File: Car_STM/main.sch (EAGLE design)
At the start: 66 parts, among them IC1 BLUEPILL550, IC2 7805TV, K1 G2R, K2 G2R, K3 TF2-L2-9V, Q1 BC557, Q2 BC557, T1 BC547, T2 BC547, T3 BC547, T4 BC547, X1 1751251, X10 1751251, X11 1751251, X2 1751248, X3 1751264, X4 1751251, X5 1751303, X6 1751248, X7 1751248, X8 1751248, X9 1751264

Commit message: V1.1 Schematic ended
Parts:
- removed C2: 100n, resistor:C-EUC2012
- removed IC2: 7805TV, linear:7805TV
- removed K2: G2R, relay:G2R
- removed T1, T2, T3, T4: BC547, transistor:BC547
- removed T5, T6, T7, T8: (no value), transistor:-NPN-TO92-ECB
- removed X11: 1751251, con-phoenix-350:1751251
- removed X8: 1751248, con-phoenix-350:1751248
- added 12V_IN: (no value), con-ptr500:AK500/3
- added D5: (no value), diode:DIODE-DO-214AC
- added D6: LL4148, _hhn_diodes_smd:LL4148
- added FUSE1: F0.315, resistor:R-EU_R2512
- added FUSE2: F1.0, resistor:R-EU_R2512
- added K4: S22, Stworzone:S22
- added Q10, Q11, Q12, Q13, Q14, Q15, Q16, Q5, Q6, Q7: BC817-40LT1SMD, transistor-npn:BC817-40LT1SMD
- added Q18, Q3, Q4, Q8: BSS123, transistor-small-signal:BSS123
- added Q9: IRFR5305, transistor-power:IRFR5305
- added R25, R29: 2k2, resistor:R-EU_R0805
- added R26, R27: 240, resistor:R-EU_R0805
- added R30: 100k, resistor:R-EU_R0805
- C1: value 100n -> 100u; device resistor:C-EUC2012 -> resistor:CPOL-EUE2,5-6E
- C3: value 100u -> (none); device resistor:CPOL-EUE2,5-6E -> Cap-Gold:CAP-13,5
- D3: value BAS15 -> (none); device diode:BAS15 -> diode:DIODE-DO-214AC
- D4: value BAS15 -> LL4148; device diode:BAS15 -> _hhn_diodes_smd:LL4148
- K1: value G2R -> G2RE; device relay:G2R -> relay:G2RE
- Q1, Q2: value BC557 -> BC807-40LT1SMD; device transistor-pnp:BC557 -> transistor-pnp:BC807-40LT1SMD
- R1, R2: value 2k2 -> 100k; device resistor:R-EU_0204/7 -> resistor:R-EU_R0805
- R10, R6: value 1k8 -> 6k8; device rcl:R-EU_0204/5 -> resistor:R-EU_R0805
- R12: value 2k2 -> 100; device resistor:R-EU_0204/7 -> resistor:R-EU_R0805
- R13, R14, R24: device resistor:R-EU_0204/7 -> resistor:R-EU_R0805
- R15: value 200 -> 240; device pot:TRIM_EU-B25P -> resistor:R-EU_R0805
- R16: value 70 -> 100; device resistor:R-EU_0204/7 -> resistor:R-EU_R0805
- R17, R3, R4: value 2k2 -> 1k8; device resistor:R-EU_0204/7 -> resistor:R-EU_R0805
- R18: value 2k2 -> 6k8; device resistor:R-EU_0204/7 -> resistor:R-EU_R0805
- R19: value 6k8 -> 1k8; device rcl:R-EU_0204/5 -> resistor:R-EU_R0805
- R20: value 1k8 -> 2k2; device rcl:R-EU_0204/5 -> resistor:R-EU_R0805
- R21, R22: value 100k -> 100; device resistor:R-EU_0204/7 -> resistor:R-EU_R0805
- R23: value 0 -> 2k2; device resistor:R-EU_0204/7 -> resistor:R-EU_R0805
- R5: device rcl:R-EU_0204/5 -> resistor:R-EU_R0805
- R9: value 6k8 -> 2k2; device rcl:R-EU_0204/5 -> resistor:R-EU_R0805
- X1: value 1751251 -> (none); device con-phoenix-350:1751251 -> con-ptr500:AK500/3
- X10: value 1751251 -> 1751264; device con-phoenix-350:1751251 -> con-phoenix-350:1751264
- X4: value 1751251 -> (none); device con-phoenix-350:1751251 -> con-ptr500:AK500/2
- X6: value 1751248 -> 1751264; device con-phoenix-350:1751248 -> con-phoenix-350:1751264
- X9: value 1751264 -> 1751277; device con-phoenix-350:1751264 -> con-phoenix-350:1751277
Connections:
- removed net +5V: C1.1, C3.+, IC2.VO, X3-3.K
- removed net BOOT_OPEN: IC1.PB7, R17.2
- removed net LOCK: IC1.PB8, R18.2
- removed net OBD_RX: IC1.PA9, X3-2.K
- removed net OBD_TX: IC1.PA10, X3-1.K
- removed net POWER_ON: R12.2
- removed net RFID_RS: IC1.PA15, X5-7.K
- new net 12_VOL: IC1.PA1, R18.1, R19.2
- new net AUDIO1: IC1.PA6, R25.1
- new net AUDIO2: IC1.PA7, R24.2
- new net BT_MODE: IC1.PB1, R29.1
- new net BT_POW: IC1.PB0, R22.1
- new net CAN_POW: IC1.PB7, R12.1
- new net CAN_RX: IC1.PB8, X3-1.K
- new net CAN_TX: IC1.PB9, X3-2.K
- new net MAIN_POW: D6.A, IC1.PC13
- new net MIR_POW: IC1.PC15, R9.1
- new net N$30: K31.O, X10-2.K
- new net N$31: K31.P, K32.S
- new net N$32: K32.O, X10-1.K
- new net N$33: K32.P, X10-4.K
- new net N$34: K3S.+, R27.1
- new net N$35: K3R.+, R26.1
- new net N$36: K3S.-, Q6.C
- new net N$37: K3R.-, Q7.C
- new net N$38: Q6.B, R25.2
- new net N$39: Q8.D, X9-4.K
- new net N$40: FUSE1.1, FUSE2.1, Q9.D
- new net N$41: Q7.B, R24.1
- new net N$42: R29.2, X9-5.K
- new net N$43: Q10.B, R20.1, R23.1
- new net N$44: Q10.C, Q9.G, R30.1
- new net N$45: D6.C, R23.2
- new net N$46: C7.1, FUSE1.2, LM1084.VI
- new net N$47: Q18.D, U$1.GND
- new net N$48: K4G$1.P, X1-3.KL
- new net N$49: C4.1, FUSE2.2, LM317.VI
- new net N$51: Q18.G, R21.2
- new net SIM_POW: IC1.PB6, R21.1
- net +12V: now also D5.C, K4G$1.S, K4G$2.1, Q9.S, R26.2, R27.2, R30.2; no longer C7.1, D4.C, K12.S, K21.1, LM1084.VI, R21.1, R22.1, X1-1.K
- net +3V3: now also C3.+, IC1.3VB, R15.2, X3-3.K, X5-7.K, X6-1.K; no longer R15.A, X10-1.K, X11-1.K
- net 12_IN: now also D4.A, IC1.PA0, R10.2, R17.1; no longer IC1.PB0, R19.1, R20.2
- net BUZZER: now also IC1.PA11
- net FUEL_POMP: now also IC1.PC14, R13.1; no longer IC1.PA8, R13.2
- net GND: now also 12V_IN-3.KL, C1.-, Q10.E, Q11.E, Q12.E, Q15.E, Q16.E, Q18.S, Q3.S, Q4.S, Q5.E, Q6.E, Q7.E, Q8.S, R17.2, R19.1, R3.2, R4.2, X6-4.K; no longer C1.2, C2.2, IC2.GND, R10.1, R20.1, R23.2, R6.1, T1.E, T2.E, T3.E, T4.E, T5.E, T6.E, T8.E, U$1.GND, X10-2.K, X11-2.K, X3-4.K, X4-3.K, X9-4.K
- net L1: now also IC1.PA2; no longer IC1.PA12, R3.2
- net L2: now also IC1.PA3, R2.1; no longer IC1.PA11, R2.2, R4.2
- net LOCK_CLOSE: now also R4.1; no longer R5.1
- net LOCK_OPEN: now also IC1.PB5, R3.1, R5.2; no longer IC1.PB3, R10.2, R9.1
- net M1: now also X6-2.K; no longer X10-3.K
- net M2: now also X6-3.K; no longer X11-3.K
- net N$1: now also 12V_IN-1.KL, R18.2; no longer X4-1.K
- net N$10: now also D4.C, R20.2; no longer R3.1, T2.B
- net N$12: now also Q3.G, R12.2; no longer C2.1, C4.1, IC2.VI, K12.P, LM317.VI
- net N$13: now also Q8.G, R22.2; no longer D4.A, K11.2, T3.C
- net N$15: now also Q3.D, X3-4.K; no longer R12.1, T3.B
- net N$16: now also K11.2, Q16.C; no longer K21.2, T4.C
- net N$17: now also Q16.B, R13.2; no longer R13.1, T4.B
- net N$18: now also K12.S, K12.S@1, X4-1.KL; no longer K22.S, X6-1.K
- net N$19: now also K12.P, K12.P@1, X4-2.KL; no longer K22.P, X6-2.K
- net N$2: now also 12V_IN-2.KL, R10.1; no longer R19.2, X4-2.K
- net N$21: now also Q4.D; no longer T8.C
- net N$22: now also K31.S, X10-3.K; no longer R15.S, R16.2
- net N$23: now also Q14.B, R1.1; no longer R17.1, T6.B
- net N$24: now also Q5.B; no longer T5.B
- net N$25: now also Q13.B, R2.2; no longer R21.2, T6.C, X8-1.K
- net N$26: now also Q11.B, Q14.E; no longer R18.1, T7.B
- net N$27: now also Q4.G, R16.2; no longer R24.1, T8.B
- net N$28: now also Q15.B, R9.2; no longer R22.2, T7.C, X8-2.K
- net N$29: now also D5.A, K4G$2.2, Q15.C; no longer R23.1, T7.E
- net N$3: now also R6.1; no longer R5.2
- net N$4: now also Q11.C, X1-2.KL; no longer T1.C, X1-2.K
- net N$5: now also Q12.C, X1-1.KL; no longer T2.C, X1-3.K
- net N$6: now also R5.1; no longer R9.2
- net N$7: now also Q14.C, Q2.B; no longer Q1.B, R1.1
- net N$8: now also Q1.B, Q13.C; no longer Q2.B, R4.1
- net N$9: now also Q12.B, Q13.E; no longer R2.1, T1.B
- net RFID_INT: now also IC1.PA12; no longer IC1.PB5
- net RFID_POW: now also IC1.PA15, R16.1; no longer R24.2
- net SIM_RS: now also IC1.PA8; no longer IC1.PA1
- net SIM_RX: now also IC1.PA9; no longer IC1.PA2
- net SIM_TX: now also IC1.PA10; no longer IC1.PA3
- net VCC: now also C1.+
- net WATER: now also IC1.PB3, Q5.C, R15.1; no longer IC1.PB6, R16.1, T5.C
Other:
- moved on the sheet: C4, C5, C6, C7, C8, D1, D2, K1, K3, LM1084, LM317, Q1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

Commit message: V1.2 Two boards from one.
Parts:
- removed IC1: BLUEPILL550, STM32BluePill:BLUEPILL550
- removed LM1084: 3V3, linear:317T
- added C10, C11, C12, C13, C2, C33, C9: 100nF, eagle-ltspice:CC2012
- added C14, C15: 100u, resistor:CPOL-EUE2,5-6E
- added C29, C30: 10pF, eagle-ltspice:CC2012
- added C31, C32: 6,8pF, eagle-ltspice:CC2012
- added D10, D11, D12, D13, D14, D15, D16, D17, D7, D8, D9: (no value), diode:DIODE-DO-214AC
- added JP1: (no value), pinhead:PINHD-1X4
- added K10, K11, K2: HY1-12V, relay:HY1-12V
- added K12, K13: G2RE, relay:G2RE
- added K14: TF2-L2-9V, relay:TF2-L2-9V
- added K5, K6, K7, K8, K9: S22, Stworzone:S22
- added LM1086: 3V3, v-reg:LM317BD2T
- added Q17: 8MHz, crystal:CRYSTALHC49UP
- added Q19: MC-306 - 32,768kHz, crystal:MC-306
- added Q20, Q21, Q22, Q23, Q24, Q25, Q26, Q27, Q28, Q29, Q30, Q31: BC817-40LT1SMD, transistor-npn:BC817-40LT1SMD
- added R28, R31, R32, R33, R34, R35, R36, R37, R38, R39, R40, R41: 2k2, resistor:R-EU_R0805
- added R42, R43: 120, resistor:R-EU_R0805
- added S1: SWITCH-MOMENTARY-2SMD-4, SparkFun-Electromechanical:SWITCH-MOMENTARY-2SMD-4
- added SJ1, SJ2, SJ3, SJ4: (no value), jumper:SJ
- added U$2, U$3, U$4, U$5: JACK_3.5, Stworzone:JACK_3.5
- added U$6, U$7: D2_HEAT, Stworzone:D2_HEAT
- added U1: STM32F10XRXT6, stm32:STM32F10XRXT6
- added X11, X13: 1751248, con-phoenix-350:1751248
- added X12, X17, X18: 1751251, con-phoenix-350:1751251
- added X14, X15, X16, X21: (no value), con-ptr500:AK500/2
- added X19, X20, X8: (no value), con-ptr500:AK500/3
- D1, D2: value 1N4004 -> (none); device diode:1N4004 -> diode:DIODE-P6-15
- LM317: value 4v2 -> 4V2; device linear:317T -> v-reg:LM317BD2T
- R26, R27: value 240 -> 120
- X1: value (none) -> 1751248; device con-ptr500:AK500/3 -> con-phoenix-350:1751248
- X10: value 1751264 -> (none); device con-phoenix-350:1751264 -> con-ptr500:AK500/2
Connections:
- removed net N$1: 12V_IN-1.KL, D1.A, R18.2
- new net AD_REL1: R33.1, U1PORTC_L.PC5
- new net AD_REL2: R34.1, U1PORTC_L.PC6
- new net AD_REL3: R35.1, U1PORTC_L.PC7
- new net AD_REL4: R36.1, U1PORTC_H.PC8
- new net AD_REL5: R37.1, U1PORTC_H.PC9
- new net AD_REL6: R38.1, U1PORTC_H.PC10
- new net AD_REL7: R39.1, U1PORTC_H.PC11
- new net BOOT0: SJ2.1, SJ3.1, U1RESET.BOOT0
- new net BOOT1: SJ1.1, SJ4.1, U1PORTB_L.PB2
- new net BT_STER: R28.1, U1PORTC_H.PC13
- new net CHAR_POW: R31.1, U1PORTC_L.PC4
- new net C_OSC1: C31.2, Q19.1, U1PORTC_H.PC14
- new net C_OSC2: C32.2, Q19.2, U1PORTC_H.PC15
- new net DAY_LIGHT: R32.1, U1PORTC_H.PC12
- new net LIGHT: U1PORTC_L.PC0, X12-2.K
- new net N$100: K141.P, U$5.2
- new net N$101: K142.P, U$5.5
- new net N$50: Q31.B, R41.1
- new net N$52: D7.A, K21.2, Q20.C
- new net N$53: Q20.B, R28.2
- new net N$54: D11.C, K6G$1.P, X13-1.K
- new net N$55: Q26.B, R36.2
- new net N$56: D8.A, K5G$2.2, Q21.C
- new net N$57: K22.S, X11-2.K
- new net N$58: K22.P, K22.P@1, X11-1.K
- new net N$59: Q21.B, R31.2
- new net N$60: D9.A, K6G$2.2, Q22.C
- new net N$61: Q22.B, R32.2
- new net N$62: D10.A, K7G$2.2, Q23.C
- new net N$63: Q23.B, R33.2
- new net N$64: K5G$1.P, X8-2.KL
- new net N$65: K7G$1.P, X14-1.KL
- new net N$66: D14.A, K101.2, Q26.C
- new net N$67: D12.A, K8G$2.2, Q24.C
- new net N$68: Q24.B, R34.2
- new net N$69: K8G$1.P, X15-1.KL
- new net N$70: Q27.B, R37.2
- new net N$71: D13.A, K9G$2.2, Q25.C
- new net N$72: Q25.B, R35.2
- new net N$73: K9G$1.P, X16-1.KL
- new net N$74: D15.A, K111.2, Q27.C
- new net N$75: Q28.B, R38.2
- new net N$76: K102.S, X17-1.K
- new net N$77: Q29.B, R39.2
- new net N$78: D17.A, K131.2, Q29.C
- new net N$79: K102.O, X17-3.K
- new net N$80: D16.A, K121.2
- new net N$81: K102.P, K102.P@1, X17-2.K
- new net N$82: K112.S, X18-1.K
- new net N$83: K112.O, X18-3.K
- new net N$84: K112.P, K112.P@1, X18-2.K
- new net N$85: K122.S, K122.S@1, X19-1.KL
- new net N$86: K122.O, K122.O@1, X19-3.KL
- new net N$87: K122.P, K122.P@1, X19-2.KL
- new net N$88: K132.S, K132.S@1, X20-1.KL
- new net N$89: K132.O, K132.O@1, X20-3.KL
- new net N$90: K132.P, K132.P@1, X20-2.KL
- new net N$91: K141.O, U$2.2
- new net N$92: K142.O, U$2.5
- new net N$93: K142.S, K32.P
- new net N$94: K141.S, K31.P
- new net N$95: K31.S, U$3.2
- new net N$96: K31.O, U$3.5
- new net N$97: K32.S, U$4.2
- new net N$98: K32.O, U$4.5
- new net N$99: U$2.1, U$3.1, U$4.1, U$5.1
- new net NRST: C33.2, S1.1, U1RESET.NRST
- new net OSC_IN: C30.2, Q17.2, U1PORTD/OSC.PD0/OSC<=
- new net OSC_OUT: C29.2, Q17.1, U1PORTD/OSC.PD1/OSC=>
- new net SWCLK: JP1.3, U1PORTA_H.PA14
- new net SWDIO: JP1.2, U1PORTA_H.PA13
- new net V+: 12V_IN-1.KL, D1.A, D10.C, D12.C, D13.C, D8.C, D9.C, K5G$1.S, K5G$2.1, K6G$1.S, K6G$2.1, K7G$1.S, K7G$2.1, K8G$1.S, K8G$2.1, K9G$1.S, K9G$2.1, R18.2, X10-1.KL, X10-2.KL
- new net VBAT: C3.+, U1AN_POWER.VBAT
- net +12V: now also D14.C, D15.C, D16.C, D17.C, D7.C, K101.1, K111.1, K121.1, K131.1, K21.1, R42.2, R43.2
- net +3V3: now also C10.2, C11.2, C12.2, C13.2, C2.2, C9.2, JP1.1, LM1086.OUT, SJ3.2, SJ4.2, U$6.K@1, U1AN_POWER.VDDA, U1POWER.VDD_1, U1POWER.VDD_2, U1POWER.VDD_3, U1POWER.VDD_4, X12-1.K; no longer C3.+, IC1.+3.3V, IC1.3.3V, IC1.3VB, LM1084.VO
- net 12_IN: now also U1PORTA_L.PA0; no longer IC1.PA0
- net 12_VOL: now also U1PORTA_L.PA1; no longer IC1.PA1
- net AUDIO1: now also R24.2, U1PORTA_L.PA6; no longer IC1.PA6
- net AUDIO2: now also R40.1, R41.2, U1PORTA_L.PA7; no longer IC1.PA7, R24.2
- net BT_MODE: now also U1PORTB_L.PB1; no longer IC1.PB1
- net BT_POW: now also U1PORTB_L.PB0; no longer IC1.PB0
- net BT_RX: now also U1PORTB_H.PB10; no longer IC1.PB10
- net BT_TX: now also U1PORTB_H.PB11; no longer IC1.PB11
- net BUZZER: now also U1PORTA_H.PA11; no longer IC1.PA11
- net CAN_POW: now also U1PORTB_L.PB7; no longer IC1.PB7
- net CAN_RX: now also U1PORTB_H.PB8; no longer IC1.PB8
- net CAN_TX: now also U1PORTB_H.PB9; no longer IC1.PB9
- net FUEL_POMP: now also U1PORTC_L.PC2; no longer IC1.PC14
- net GND: now also C10.1, C11.1, C12.1, C13.1, C14.-, C15.-, C2.1, C29.1, C30.1, C31.1, C32.1, C33.1, C9.1, D11.A, JP1.4, LM1086.ADJ, Q20.E, Q21.E, Q22.E, Q23.E, Q24.E, Q25.E, Q26.E, Q27.E, Q28.E, Q29.E, Q30.E, Q31.E, S1.2, SJ1.2, SJ2.2, U1AN_POWER.VSSA, U1POWER.VSS_1, U1POWER.VSS_2, U1POWER.VSS_3, U1POWER.VSS_4, X12-3.K, X13-2.K, X14-2.KL, X15-2.KL, X16-2.KL, X21-1.KL, X21-2.KL, X8-3.KL; no longer IC1.GND, IC1.GND1, IC1.GND2, LM1084.ADJ
- net L1: now also U1PORTA_L.PA2; no longer IC1.PA2
- net L2: now also U1PORTA_L.PA3; no longer IC1.PA3
- net LOCK_CLOSE: now also U1PORTB_L.PB4; no longer IC1.PB4
- net LOCK_OPEN: now also U1PORTB_L.PB5; no longer IC1.PB5
- net M1: now also U1PORTA_L.PA4; no longer IC1.PA4
- net M2: now also U1PORTA_L.PA5; no longer IC1.PA5
- net MAIN_POW: now also U1PORTC_L.PC1; no longer IC1.PC13
- net MIR_POW: now also U1PORTC_L.PC3; no longer IC1.PC15
- net N$22: now also K14S.+, R43.1; no longer K31.S, X10-3.K
- net N$30: now also K14R.+, R42.1; no longer K31.O, X10-2.K
- net N$31: now also K14S.-, Q30.C; no longer K31.P, K32.S
- net N$32: now also K14R.-, Q31.C; no longer K32.O, X10-1.K
- net N$33: now also Q30.B, R40.2; no longer K32.P, X10-4.K
- net N$4: now also X1-2.K; no longer X1-2.KL
- net N$46: now also C14.+, LM1086.IN; no longer LM1084.VI
- net N$48: now also X8-1.KL; no longer X1-3.KL
- net N$49: now also C15.+, LM317.IN; no longer LM317.VI
- net N$5: now also X1-1.K; no longer X1-1.KL
- net RFID_CS: now also U1PORTB_H.PB12; no longer IC1.PB12
- net RFID_INT: now also U1PORTA_H.PA12; no longer IC1.PA12
- net RFID_MISO: now also U1PORTB_H.PB14; no longer IC1.PB14
- net RFID_MOSI: now also U1PORTB_H.PB15; no longer IC1.PB15
- net RFID_POW: now also U1PORTA_H.PA15; no longer IC1.PA15
- net RFID_SCK: now also U1PORTB_H.PB13; no longer IC1.PB13
- net SIM_POW: now also U1PORTB_L.PB6; no longer IC1.PB6
- net SIM_RS: now also U1PORTA_H.PA8; no longer IC1.PA8
- net SIM_RX: now also U1PORTA_H.PA9; no longer IC1.PA9
- net SIM_TX: now also U1PORTA_H.PA10; no longer IC1.PA10
- net VCC: now also LM317.OUT, U$7.K@1; no longer LM317.VO
- net WATER: now also U1PORTB_L.PB3; no longer IC1.PB3
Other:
- moved on the sheet: 12V_IN-3, C1, C3, C4, C5, C6, C7, C8, D5, K3, K4, Q1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

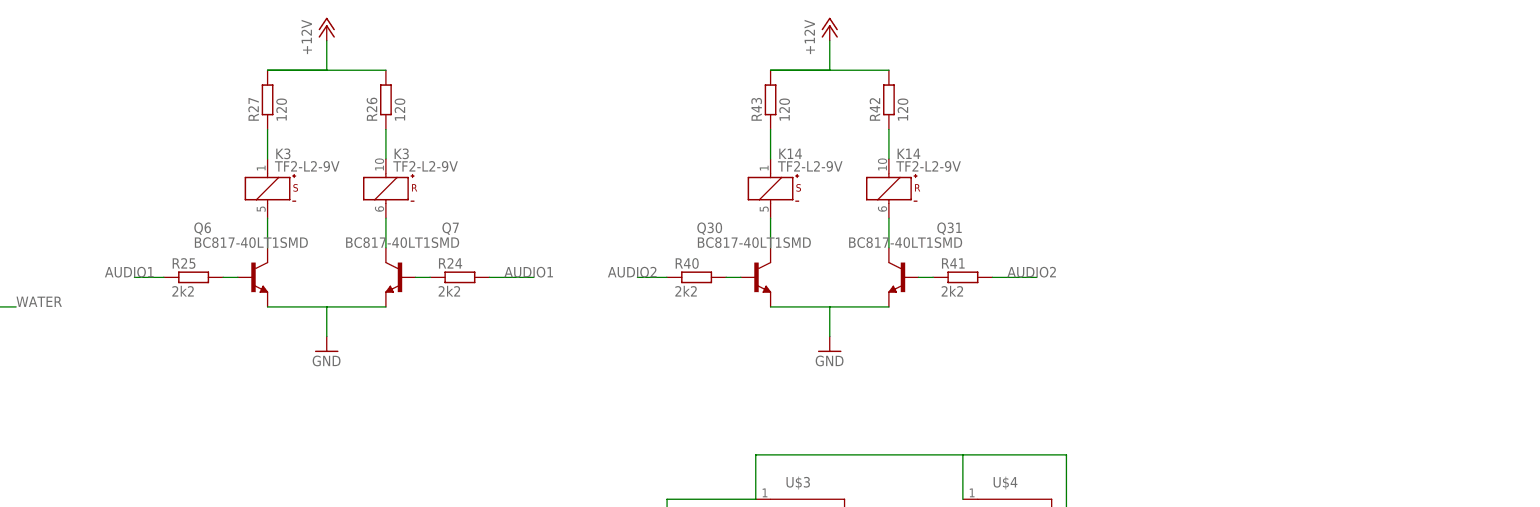
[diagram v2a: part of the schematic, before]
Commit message: V1.21 New BT, audio, big cap on 12V
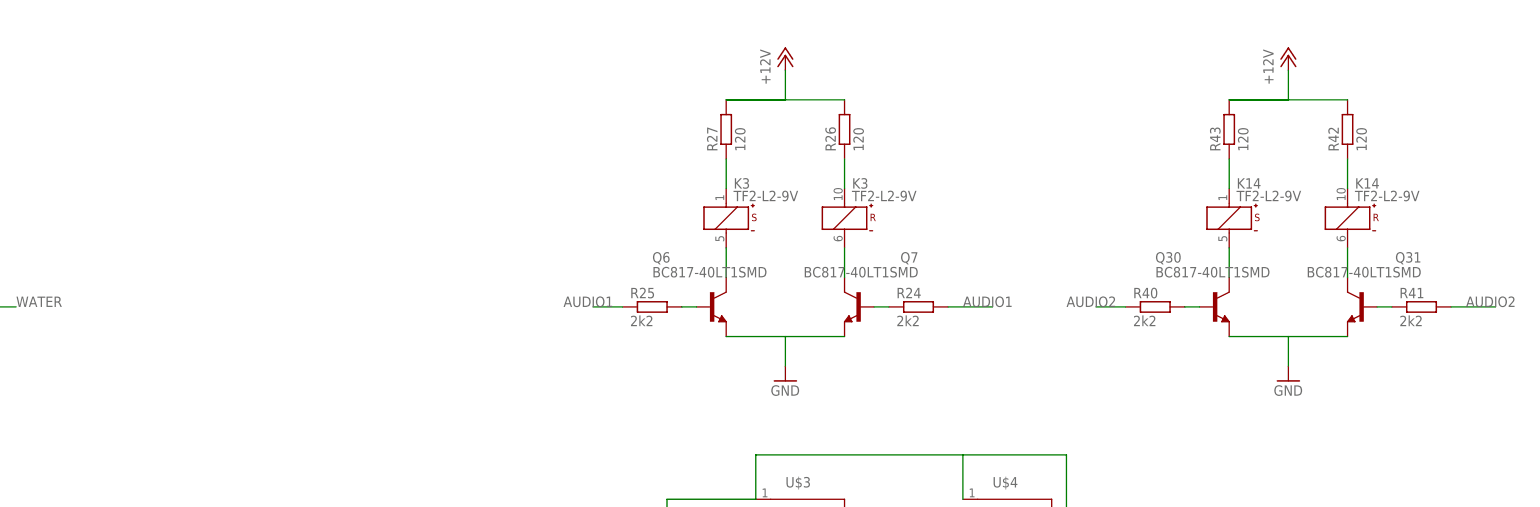
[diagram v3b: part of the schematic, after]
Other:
- moved on the sheet: K14, K3, Q30, Q31, Q6, Q7, R24, R25, R26, R27, R40, R41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
